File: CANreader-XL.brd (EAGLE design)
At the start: 79.8 x 49.8 mm, 77 parts, among them IC1 MCP2551, IC2 TJA1055T/3, IC3 BD9G101G, IC4 LM1117IMPX-3.3, IC5 STM32F107VBT, Q1 16MHz, SW1 SLEEP, SW2 TERM, U1 HC_05, X1 MINI-USB, X2 SWD, X3 GPIO, X4 UART, X5 CAN, X6 LAN

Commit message: LQFP100 -> LQFP64 in schematics
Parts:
- removed C8: 0.1uF, rcl:C0805
- removed IC5: STM32F107VBT, micro-stm_v2:LQFP100
- removed R18, R19, R20, R24: 0, rcl:R0805
- added IC6: STM32F107RBT, micro-stm_v2:LQFP64
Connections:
- removed net MCO: IC5.67, R18.1
- removed net N$37: R18.2, R19.2, X6.13
- removed net PA0: IC5.23, X6.2
- removed net PA7: IC5.32, X3.1
- removed net PB10: IC5.47, X6.6
- removed net PB14: IC5.53, X6.8
- removed net PB15: IC5.54, X6.5
- removed net PD3: IC5.84, X6.3
- removed net PD4: IC5.85, X6.4
- removed net PD7: IC5.88, X6.1
- removed net VREF+: IC5.21, R20.2
- removed net VREF-: IC5.20, R24.2
- new net PA3: IC6.17, X3.5
- net +3V3: now also IC6.1, IC6.13, IC6.19, IC6.32, IC6.48, IC6.64; no longer C8.1, IC5.100, IC5.11, IC5.22, IC5.28, IC5.50, IC5.6, IC5.75, R20.1
- net CAN1_RX: now also IC6.61; no longer IC5.81
- net CAN1_TX: now also IC6.62; no longer IC5.82
- net CAN2_RX: now also IC6.57; no longer IC5.91
- net CAN2_TX: now also IC6.58; no longer IC5.92
- net GND: now also IC6.12, IC6.18, IC6.31, IC6.47, IC6.63; no longer C8.2, IC5.10, IC5.19, IC5.27, IC5.49, IC5.74, IC5.99, R24.1
- net HC_KEY: now also IC6.50; no longer IC5.77
- net HC_RESET: now also IC6.43; no longer IC5.69
- net N$1: now also IC6.5; no longer IC5.12
- net N$2: now also IC6.6; no longer IC5.13
- net N$3: now also IC6.60; no longer IC5.94
- net N$4: now also IC6.28; no longer IC5.37
- net N$6: now also IC6.41; no longer IC5.63
- net NRST: now also IC6.7; no longer IC5.14
- net PA4: now also IC6.20, X3.4; no longer IC5.29, X3.5
- net PA5: now also IC6.21, X3.3; no longer IC5.30, X3.4
- net PA6: now also IC6.22, X3.1; no longer IC5.31, X3.3
- net RMII_CRS_DV: now also IC6.23; no longer IC5.55
- net RMII_MDC: now also IC6.9; no longer IC5.16
- net RMII_MDIO: now also IC6.16; no longer IC5.25
- net RMII_REF_CLK: now also IC6.15, X6.13; no longer IC5.24, R19.1
- net RMII_RXD0: now also IC6.24; no longer IC5.56
- net RMII_RXD1: now also IC6.25; no longer IC5.57
- net RMII_TXD0: now also IC6.33; no longer IC5.51
- net RMII_TXD1: now also IC6.34; no longer IC5.52
- net RMII_TX_EN: now also IC6.30; no longer IC5.48
- net SWCLK: now also IC6.49; no longer IC5.76
- net SWDIO: now also IC6.46; no longer IC5.72
- net TJA_EN: now also IC6.55; no longer IC5.86
- net TJA_ERR: now also IC6.59; no longer IC5.96
- net TJA_STB: now also IC6.56; no longer IC5.87
- net UART4_RX: now also IC6.52; no longer IC5.79
- net UART4_TX: now also IC6.51; no longer IC5.78
- net UART5_RX: now also IC6.54; no longer IC5.83
- net UART5_TX: now also IC6.53; no longer IC5.80
- net USB_D+: now also IC6.45; no longer IC5.71
- net USB_D-: now also IC6.44; no longer IC5.70
- net USB_VBUS: now also IC6.42; no longer IC5.68
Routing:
- net PD3: track 59.1 -> 0.00 mm, vias 1 -> 0
- net PD4: track 51.4 -> 0.00 mm, vias 1 -> 0
- net N$6: track 47.9 -> 0.00 mm, vias 1 -> 0
- net +3V3: track 382.5 -> 342.5 mm, vias 12 -> 11
- net PD7: track 39.5 -> 0.00 mm, vias 1 -> 0
- net PB15: track 27.2 -> 0.00 mm, vias 1 -> 0
- net GND: track 934.2 -> 907.6 mm, vias 11 -> 10
- net PB14: track 22.9 -> 0.00 mm
- net PA7: track 22.2 -> 0.00 mm
- net PA3: track 0.00 -> 21.2 mm
- net PB10: track 20.0 -> 0.00 mm, vias 1 -> 0
- net N$4: track 19.7 -> 0.00 mm, vias 1 -> 0
- net PA0: track 16.9 -> 0.00 mm, vias 1 -> 0
- net RMII_REF_CLK: track 25.6 -> 9.48 mm, vias 3 -> 1
- net MCO: track 14.1 -> 0.00 mm, vias 1 -> 0
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
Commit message: Ethernet initial
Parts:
- added C28, C30, C32, C33, C34, C36, C37, C8: 0.1uF, rcl:C0805
- added C31: 0.01uF, rcl:C0805
- added C35: 10uF, rcl:C0805
- added C38, C39: 1uF, rcl:C0805
- added IC7: DP83848I, STM32_CAN-USB:LQFP48
- added QG1: 50MHz, crystal:SM77H
- added R18: 10K, rcl:R0805
- added R19, R20, R30, R31: 2K2, rcl:R0805
- added R24, R25, R26, R27, R34: 18, rcl:R0805
- added R28, R29: 330, rcl:R0805
- added R32: 4K7, rcl:R0805
- added R33: 150, rcl:R0805
- added X7: J11012F21K, con-pulse:J1
- Q1: value 16MHz -> 25MHz
- moved IC6 79.1 mm to (52.8, 34.8)
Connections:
- new net LEDACT_LINK: IC7.26, R28.2
- new net LED_LINK: IC7.28, R29.2
- new net N$16: IC7.29, R18.1
- new net N$17: IC7.20, R30.1
- new net N$20: IC7.39, R20.2
- new net N$21: IC7.21, R31.1
- new net N$22: R28.1, X7.9
- new net N$23: R29.1, X7.11
- new net N$24: IC7.34, QG1.3
- new net N$26: IC7.24, R32.1
- new net N$27: R32.2, R33.2
- new net N$28: R33.1, R34.1
- new net PFB: C32.1, C33.1, C34.1, C35.1, IC7.18, IC7.23, IC7.37
- new net RD+: IC7.14, R26.2, X7.4
- new net RD-: IC7.13, R27.1, X7.6
- new net TD+: IC7.17, R24.2, X7.1
- new net TD-: IC7.16, R25.1, X7.3
- net +3V3: now also C28.1, C30.1, C31.1, C36.1, C37.1, C38.1, C39.1, C8.1, IC7.22, IC7.32, IC7.48, QG1.4, R18.2, R19.1, R20.1, R24.1, R25.2, R26.1, R27.2, R30.2, R31.2, X7.10, X7.12, X7.2, X7.5
- net GND: now also C28.2, C30.2, C31.2, C32.2, C33.2, C34.2, C35.2, C36.2, C37.2, C38.2, C39.2, C8.2, IC7.15, IC7.19, IC7.35, IC7.36, IC7.47, QG1.2, R34.2, X7.8
- net RMII_CRS_DV: now also IC7.40, R19.2
- net RMII_MDC: now also IC7.31
- net RMII_MDIO: now also IC7.30
- net RMII_RXD0: now also IC7.43, IC7.44
- net RMII_TXD0: now also IC7.3
- net RMII_TXD1: now also IC7.4
- net RMII_TX_EN: now also IC7.2

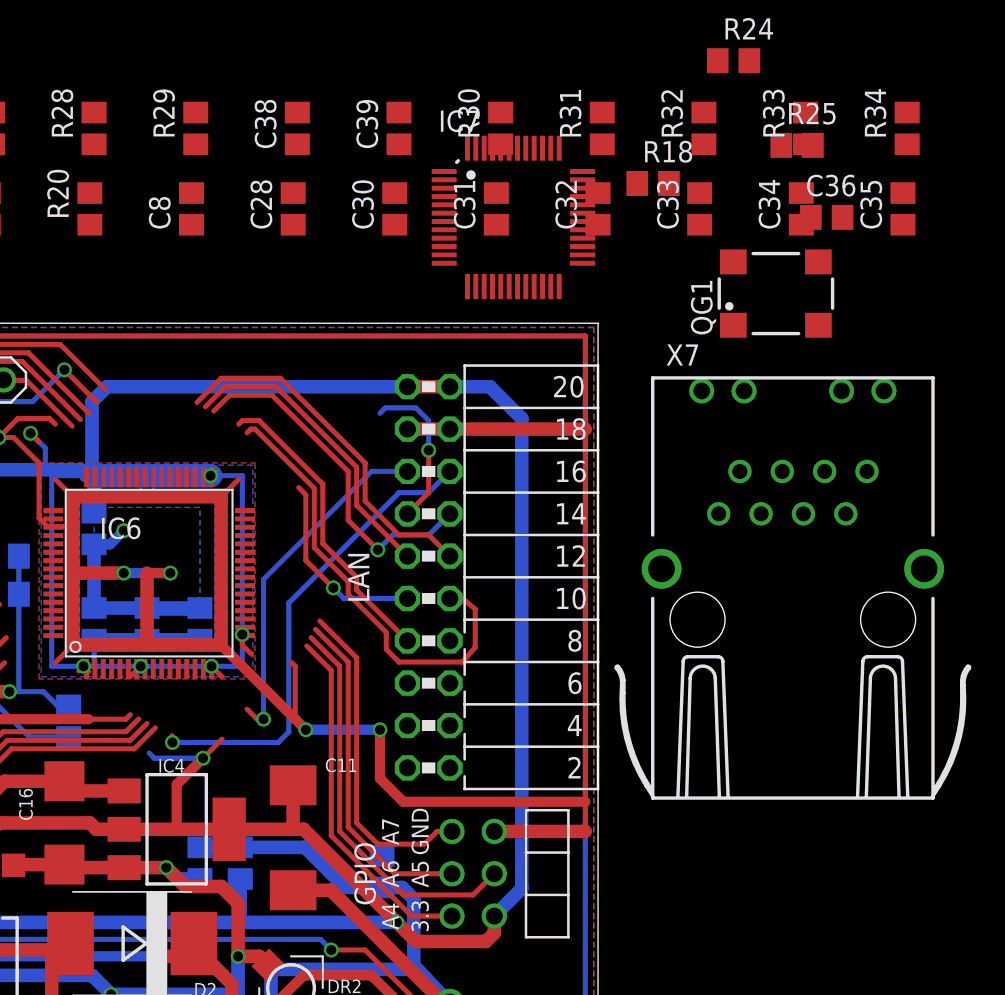
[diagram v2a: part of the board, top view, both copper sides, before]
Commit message: RJ45 connector
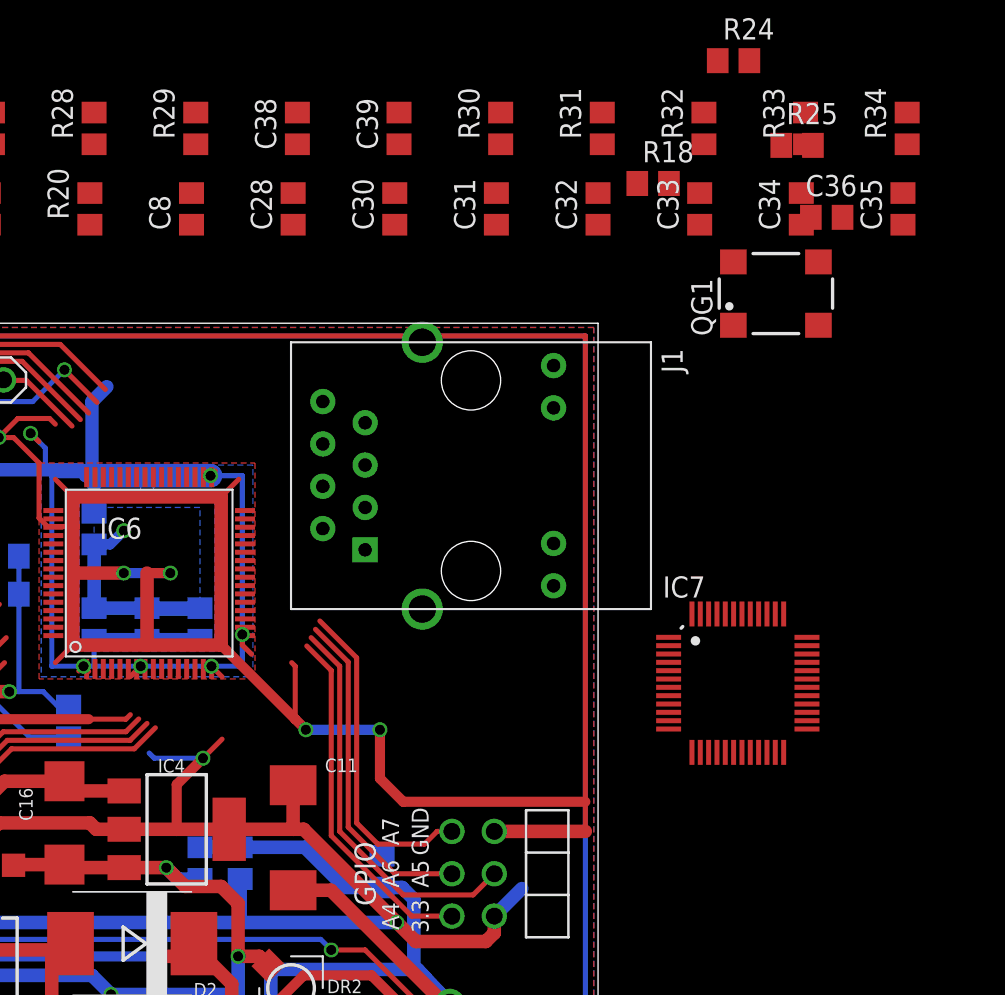
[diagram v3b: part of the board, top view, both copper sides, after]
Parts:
- removed X6: LAN, con-lsta:FE10-2W
- removed X7: J11012F21K, con-pulse:J1
- added J1: (no value), Connector:RJ45
- moved IC7 31.0 mm to (88.1, 28.2)
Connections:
- removed net N$24: IC7.34, QG1.3
- new net N$29: J1.TD-
- new net N$30: J1.P5
- net +3V3: now also J1.G+, J1.Y+; no longer X6.19, X6.20, X7.10, X7.12, X7.2, X7.5
- net GND: now also J1.GND, J1.SHIELD0, J1.SHIELD1; no longer X6.17, X6.18, X7.8
- net N$22: now also J1.G-, R29.1; no longer R28.1, X7.9
- net N$23: now also J1.Y-, R28.1; no longer R29.1, X7.11
- net RD+: now also J1.RD+; no longer X7.4
- net RD-: now also J1.RD-; no longer X7.6
- net RMII_CRS_DV: no longer X6.14
- net RMII_MDC: no longer X6.16
- net RMII_MDIO: no longer X6.15
- net RMII_REF_CLK: now also IC7.34, QG1.3; no longer X6.13
- net RMII_RXD0: no longer IC7.44, X6.11
- net RMII_RXD1: now also IC7.44; no longer X6.12
- net RMII_TXD0: no longer X6.10
- net RMII_TXD1: no longer X6.7
- net RMII_TX_EN: no longer X6.9
- net TD+: now also J1.TD+; no longer X7.1
- net TD-: no longer X7.3
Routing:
- net +3V3: track 342.5 -> 288.6 mm
- net RMII_MDC: track 28.3 -> 0.00 mm, vias 1 -> 0
- net RMII_TXD0: track 27.1 -> 0.00 mm
- net RMII_RXD1: track 21.5 -> 0.00 mm
- net RMII_CRS_DV: track 21.0 -> 0.00 mm, vias 1 -> 0
- net RMII_MDIO: track 20.9 -> 0.00 mm, vias 1 -> 0
- net RMII_TXD1: track 18.2 -> 0.00 mm
- net RMII_RXD0: track 18.2 -> 0.00 mm
- net RMII_TX_EN: track 11.6 -> 0.00 mm, vias 1 -> 0
- net GND: track 907.6 -> 896.9 mm
- net RMII_REF_CLK: track 9.48 -> 0.00 mm, vias 1 -> 0

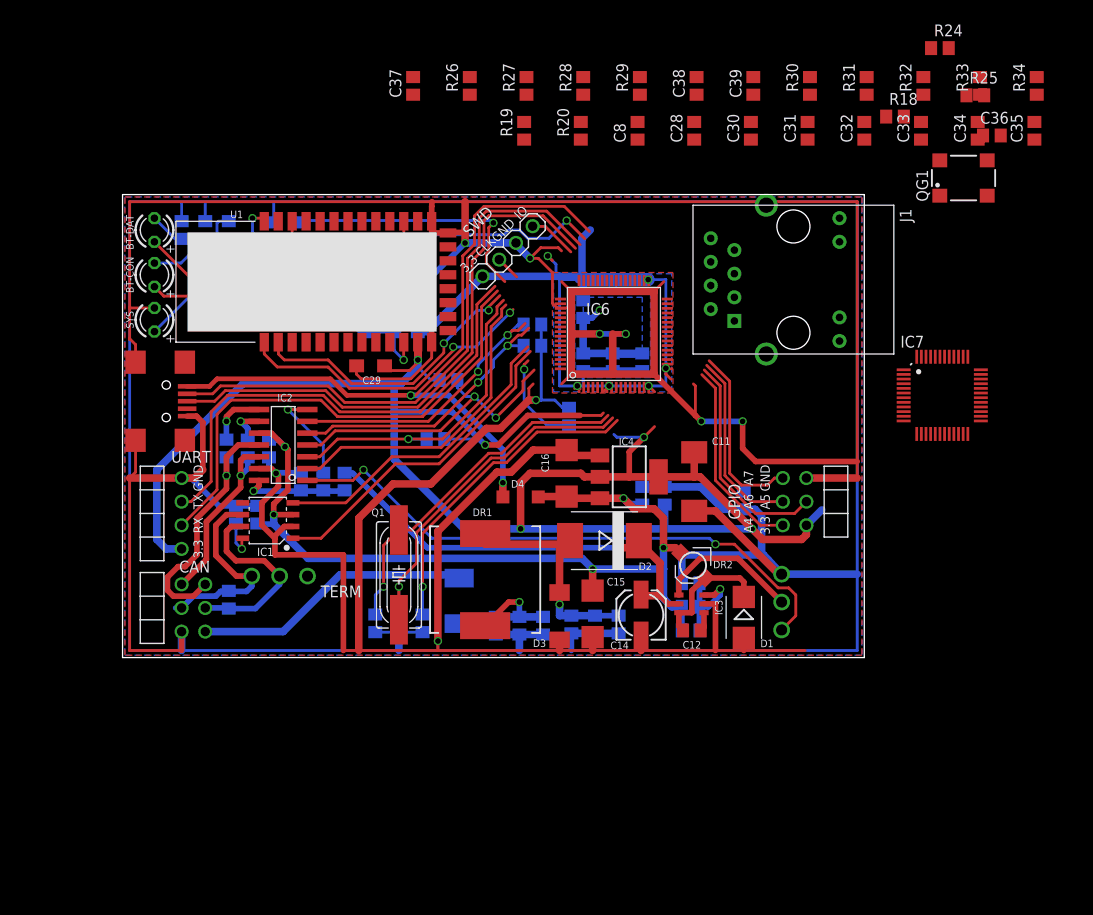
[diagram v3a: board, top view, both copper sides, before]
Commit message: fix sleep mode switch error
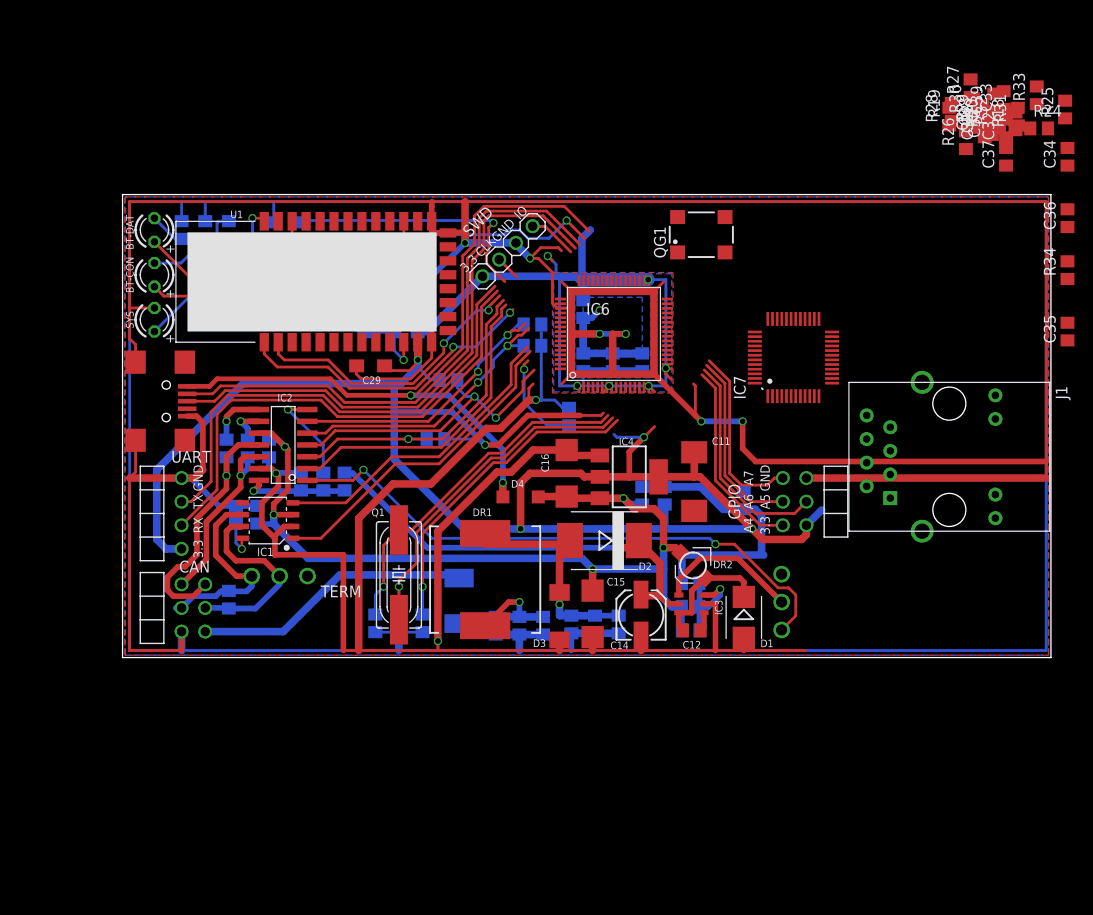
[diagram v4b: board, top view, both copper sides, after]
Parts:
- moved C37 64.2 mm to (95.0, 53.8)
- moved R26 53.7 mm to (90.7, 55.6)
- moved R27 47.8 mm to (91.2, 61.2)
- moved R19 46.0 mm to (89.2, 58.7)
- moved R20 44.0 mm to (93.2, 57.7)
- moved R28 39.5 mm to (88.9, 58.2)
- moved C8 36.9 mm to (92.2, 57.9)
- moved R29 36.7 mm to (92.2, 58.2)
- moved C28 31.3 mm to (92.7, 57.7)
- moved C38 30.9 mm to (92.5, 58.4)
- moved QG1 28.8 mm to (62.2, 45.5)
- moved C39 26.0 mm to (93.7, 59.7)
- moved C30 25.9 mm to (93.5, 57.1)
- moved J1 25.4 mm to (88.9, 21.6)
- moved C35 21.9 mm to (101.6, 35.1)
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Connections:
- net BAT: now also SW1.3
- net GND: no longer SW1.3
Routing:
- net GND: track 896.9 -> 974.3 mm
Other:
- board size 79.8 x 49.8 mm -> 99.8 x 49.8 mm
- board text added: "v0.2"
- board text removed: "v0.1"

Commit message: MCP2562, usb connector
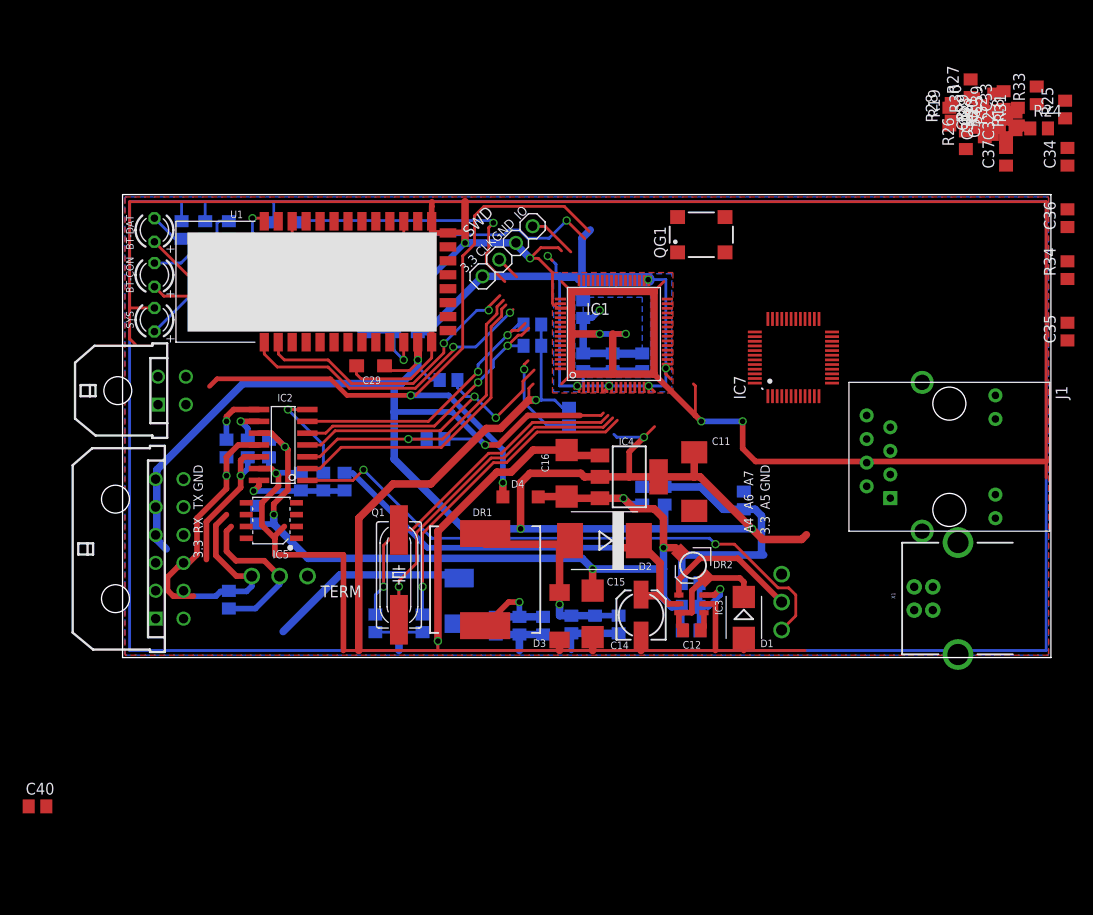
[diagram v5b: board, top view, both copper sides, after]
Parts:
- removed IC6: STM32F107RBT, micro-stm_v2:LQFP64
- removed R6: 10K, rcl:R0805
- removed X5: CAN, STM32_CAN-USB:2X03/90
- added C40: 0.1uF, rcl:C0805
- added IC5: MCP2562-SOIC8, STM32_CAN-USB:SOIC8-1.27-5X4MM
- IC1: value MCP2551 -> STM32F107RBT; device STM32_CAN-USB:SOIC8-1.27-5X4MM -> micro-stm_v2:LQFP64
- X1: value MINI-USB -> ST-USB-009A; device STM32_CAN-USB:UX60-MB-5ST -> Seeed-OPL-Connector:USB4+2-2.5-90D
- X3: value GPIO -> CAN+GPIO; device STM32_CAN-USB:2X03/90 -> con-molex-micro-fit-3_0:43045-1200
- X4: device STM32_CAN-USB:1X04/90 -> con-molex-micro-fit-3_0:43045-0400
- moved X1 85.1 mm to (87.1, 6.35), turned to 180 degrees
- moved X3 78.3 mm to (-0.76, 11.7)
- moved IC1 42.3 mm to (52.8, 34.8), turned to 0 degrees
- moved X4 13.6 mm to (-0.51, 28.7), turned to 270 degrees
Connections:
- removed net N$5: IC1.8, R6.1
- new net CAN2_STBY: IC1.29, IC5.8
- net +12V: now also X3.P$7; no longer X5.1
- net +3V3: now also C40.2, IC1.1, IC1.13, IC1.19, IC1.32, IC1.48, IC1.64, IC5.5, X3.P$10, X4.P$1; no longer IC6.1, IC6.13, IC6.19, IC6.32, IC6.48, IC6.64, X3.6, X4.1
- net +5V: now also IC5.3; no longer IC1.3
- net CAN1H: now also X3.P$9; no longer X5.5
- net CAN1L: now also X3.P$3; no longer X5.6
- net CAN1_RX: now also IC1.61; no longer IC6.61
- net CAN1_TX: now also IC1.62; no longer IC6.62
- net CAN2H: now also IC5.7, X3.P$8; no longer IC1.7, X5.3
- net CAN2L: now also IC5.6, X3.P$2; no longer IC1.6, X5.4
- net CAN2_RX: now also IC1.57, IC5.4; no longer IC1.4, IC6.57
- net CAN2_TX: now also IC1.58, IC5.1; no longer IC1.1, IC6.58
- net GND: now also C40.1, IC1.12, IC1.18, IC1.31, IC1.47, IC1.63, IC5.2, X1.GND, X1.S1, X1.S2, X3.P$1, X3.P$4, X4.P$4; no longer IC1.2, IC6.12, IC6.18, IC6.31, IC6.47, IC6.63, R6.2, X1.5, X1.M1, X1.M2, X3.2, X4.4, X5.2
- net HC_KEY: now also IC1.50; no longer IC6.50
- net HC_RESET: now also IC1.43; no longer IC6.43
- net N$1: now also IC1.5; no longer IC6.5
- net N$2: now also IC1.6; no longer IC6.6
- net N$3: now also IC1.60; no longer IC6.60
- net N$4: now also IC1.28; no longer IC6.28
- net N$6: now also IC1.41; no longer IC6.41
- net NRST: now also IC1.7; no longer IC6.7
- net PA3: now also IC1.17, X3.P$11; no longer IC6.17, X3.5
- net PA4: now also IC1.20, X3.P$12; no longer IC6.20, X3.4
- net PA5: now also IC1.21, X3.P$5; no longer IC6.21, X3.3
- net PA6: now also IC1.22, X3.P$6; no longer IC6.22, X3.1
- net RMII_CRS_DV: now also IC1.23; no longer IC6.23
- net RMII_MDC: now also IC1.9; no longer IC6.9
- net RMII_MDIO: now also IC1.16; no longer IC6.16
- net RMII_REF_CLK: now also IC1.15; no longer IC6.15
- net RMII_RXD0: now also IC1.24; no longer IC6.24
- net RMII_RXD1: now also IC1.25; no longer IC6.25
- net RMII_TXD0: now also IC1.33; no longer IC6.33
- net RMII_TXD1: now also IC1.34; no longer IC6.34
- net RMII_TX_EN: now also IC1.30; no longer IC6.30
- net SWCLK: now also IC1.49; no longer IC6.49
- net SWDIO: now also IC1.46; no longer IC6.46
- net TJA_EN: now also IC1.55; no longer IC6.55
- net TJA_ERR: now also IC1.59; no longer IC6.59
- net TJA_STB: now also IC1.56; no longer IC6.56
- net UART4_RX: now also IC1.52, X4.P$2; no longer IC6.52, X4.2
- net UART4_TX: now also IC1.51, X4.P$3; no longer IC6.51, X4.3
- net UART5_RX: now also IC1.54; no longer IC6.54
- net UART5_TX: now also IC1.53; no longer IC6.53
- net USB_D+: now also IC1.45, X1.D+; no longer IC6.45, X1.3
- net USB_D-: now also IC1.44, X1.D-; no longer IC6.44, X1.2
- net USB_VBUS: now also IC1.42, X1.VBUS; no longer IC6.42, X1.1
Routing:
- net GND: track 974.3 -> 888.5 mm
- net USB_D-: track 61.0 -> 0.00 mm
- net USB_D+: track 60.5 -> 0.00 mm
- net UART4_RX: track 53.8 -> 0.00 mm
- net UART4_TX: track 52.4 -> 0.00 mm
- net CAN2_TX: track 35.2 -> 0.00 mm
- net CAN2_RX: track 33.6 -> 0.00 mm
- net PA4: track 23.7 -> 0.00 mm
- net PA3: track 21.2 -> 0.00 mm
- net PA5: track 20.8 -> 0.00 mm
- net PA6: track 19.6 -> 0.00 mm
- net +12V: track 29.9 -> 21.6 mm
- net +3V3: track 288.6 -> 283.6 mm
- net N$5: track 4.18 -> 0.00 mm, vias 1 -> 0
- net CAN2L: track 21.7 -> 17.5 mm
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
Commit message: CAN2_STBY, Heap size
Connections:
- net CAN2_STBY: now also IC1.2; no longer IC1.29
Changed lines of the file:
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@@
 <signal name="CAN2_STBY">
 <contactref element="IC5" pad="8"/>
-<contactref element="IC1" pad="29"/>
-<wire x1="13.302" y1="12.827" x2="58.582" y2="37.048" width="0" layer="19" extent="1-1"/>
+<contactref element="IC1" pad="2"/>
+<wire x1="13.302" y1="12.827" x2="49.582" y2="29.048" width="0" layer="19" extent="1-1"/>
 </signal>
 </signals>
